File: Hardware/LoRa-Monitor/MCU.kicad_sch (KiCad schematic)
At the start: 46 parts, among them J2 Micro_SD_Card, U10 ESP32-S3-WROOM-1

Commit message: Fixed schematics and started layout
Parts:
- added GP0, RESET1, USR_INPUT1: SW_Push, Button_Switch_SMD:SW_Push_1P1T_NO_CK_KMR2, symbol Switch:SW_Push
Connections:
- net CS_SD: now also R8.1; no longer R18.2
- net ESP_EN: now also RESET1.2
- net GND: now also GP0.1, RESET1.1, USR_INPUT1.1
- net GPIO0: now also GP0.2
- net SDO_SPI1: now also R18.2; no longer R8.1
- net USR_IN: now reaches R46.2, R97.1
- net USR_IN: now also USR_INPUT1.2

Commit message: Added parameters for the productions files, changed components on LCSC to reduce the price of BoM, minimal changes on the routing.
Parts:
- added C58: 100nF, Capacitor_SMD:C_0805_2012Metric, symbol Device:C
- C43, C45, C47: value 100nF -> 100nF 50V X7R; LCSC Part # (none) -> C49678
- C44, C46: LCSC Part # (none) -> C15850
- D6: FT Rotation Offset (none) -> 180; LCSC Part # (none) -> C2886570
- GP0, RESET1, USR_INPUT1: FT Position Offset (none) -> 0,0.3175; LCSC Part # (none) -> C72443
- J2: FT Position Offset (none) -> 0,0.508; FT Rotation Offset (none) -> 180; LCSC Part # (none) -> C164170
- R0, R1, R10, R11, R12, R13, R14, R15, R16, R17, R18, R2, R21, R3, R35, R36, R37, R38, R39, R4, R40, R41, R42, R45, R46, R47, R48, R5, R6, R7, R8, R9, RRX1, RTX1: LCSC Part # (none) -> C21189
- R101, R115, R96, R97: LCSC Part # (none) -> C17414
- U10: FT Position Offset (none) -> 0,-3.65125; LCSC Part # (none) -> C2913205
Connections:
- net GND: now also C58.2
- net USR_IN: now also C58.1
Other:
- moved on the sheet: R115

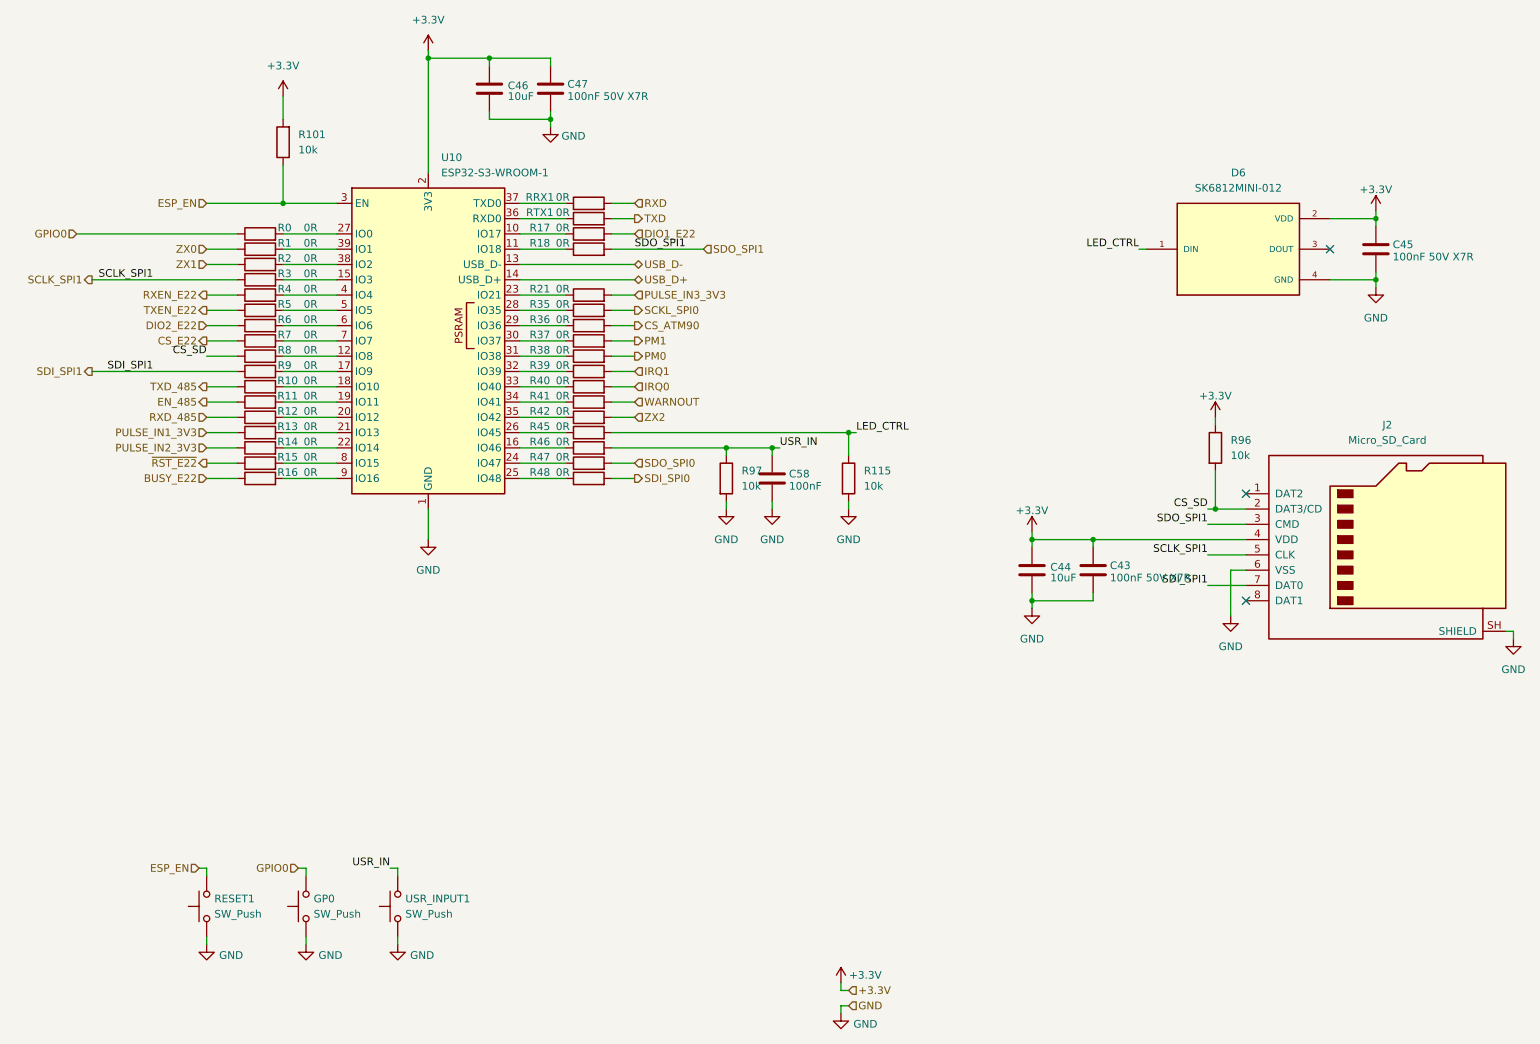
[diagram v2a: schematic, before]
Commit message: Changed the RS485-TTL translator and its relevent componentes (Power source and optocuplers) for a simpler and easier solution using the ADM2582.
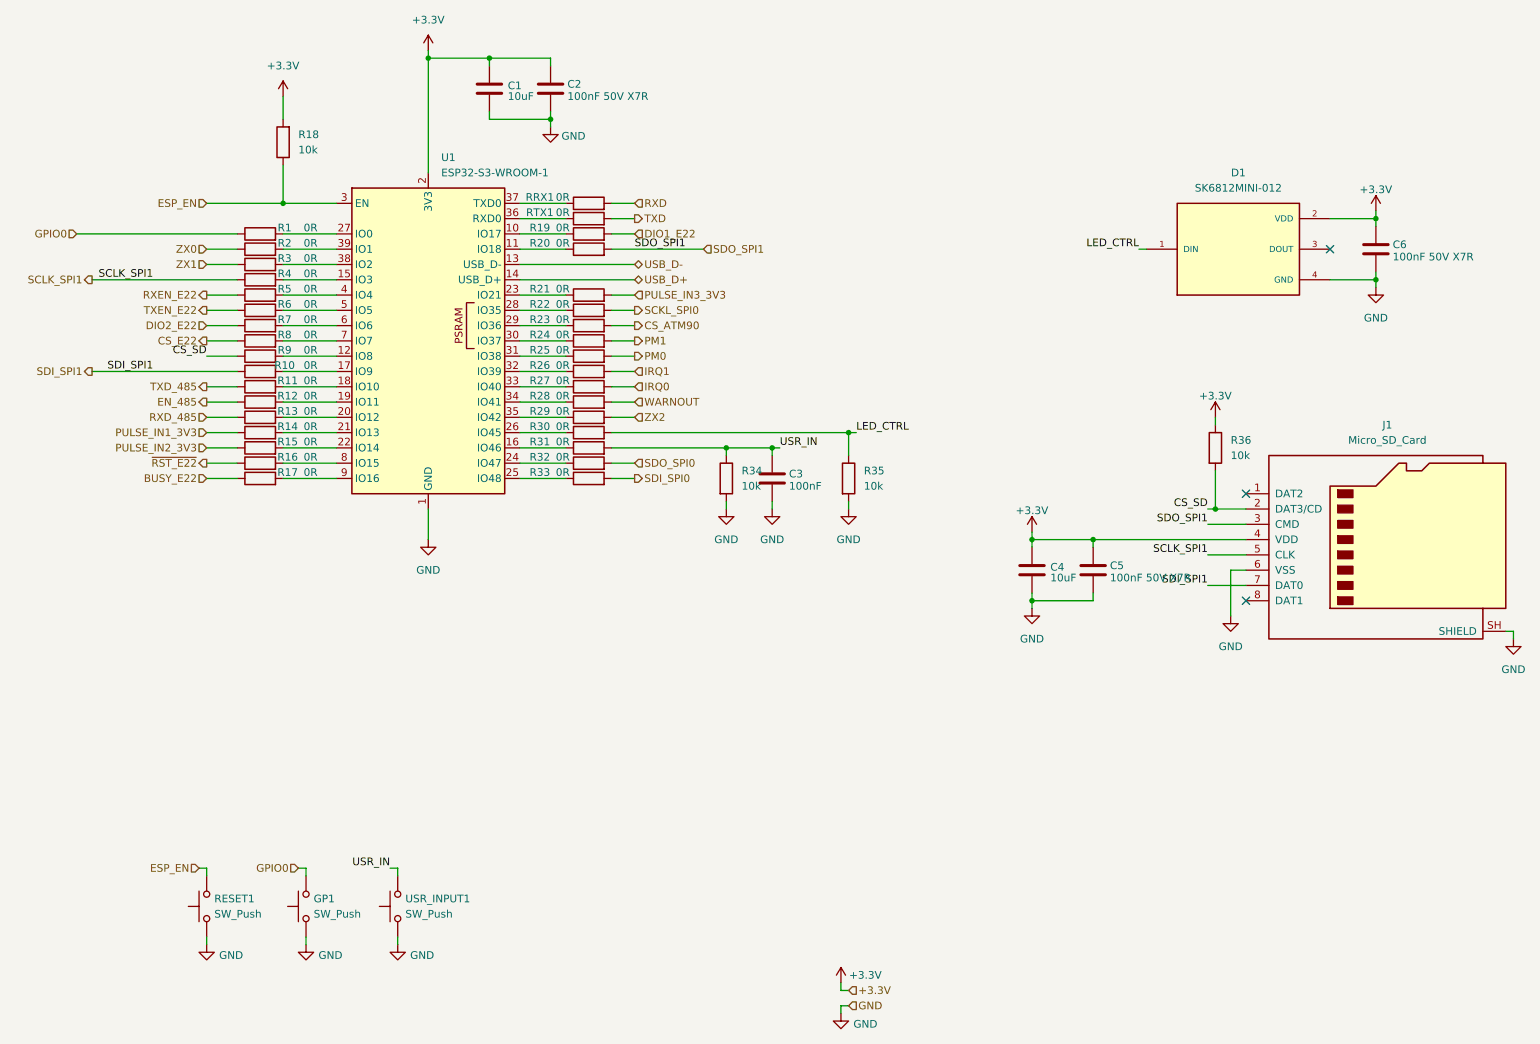
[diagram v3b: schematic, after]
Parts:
- renumbered C46 to C1, C47 to C2, C58 to C3, C44 to C4, C43 to C5, C45 to C6, D6 to D1, GP0 to GP1, J2 to J1, R0 to R1, R9 to R10, R10 to R11, R11 to R12, R12 to R13, R13 to R14, R14 to R15, R15 to R16, R16 to R17, R101 to R18, R17 to R19, R1 to R2, R18 to R20, R35 to R22, R36 to R23, R37 to R24, R38 to R25, R39 to R26, R40 to R27, R41 to R28, R42 to R29, R2 to R3, R45 to R30, R46 to R31, R47 to R32, R48 to R33, R97 to R34, R115 to R35, R96 to R36, R3 to R4, R4 to R5, R5 to R6, R6 to R7, R7 to R8, R8 to R9, U10 to U1
